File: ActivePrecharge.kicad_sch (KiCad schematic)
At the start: 52 parts, among them Con1 LED, J1 Conn_01x03, J2 Conn_01x02, J3 Conn_01x02, Q1 IRLML0030, U1 NCP785AH50T1G, U1I_TP1 TestPoint, U2 NCP785AH50T1G, U2I_TP1 TestPoint, U2O_TP1 TestPoint, U3 TLV9301xDCK, U4 TCMT1106

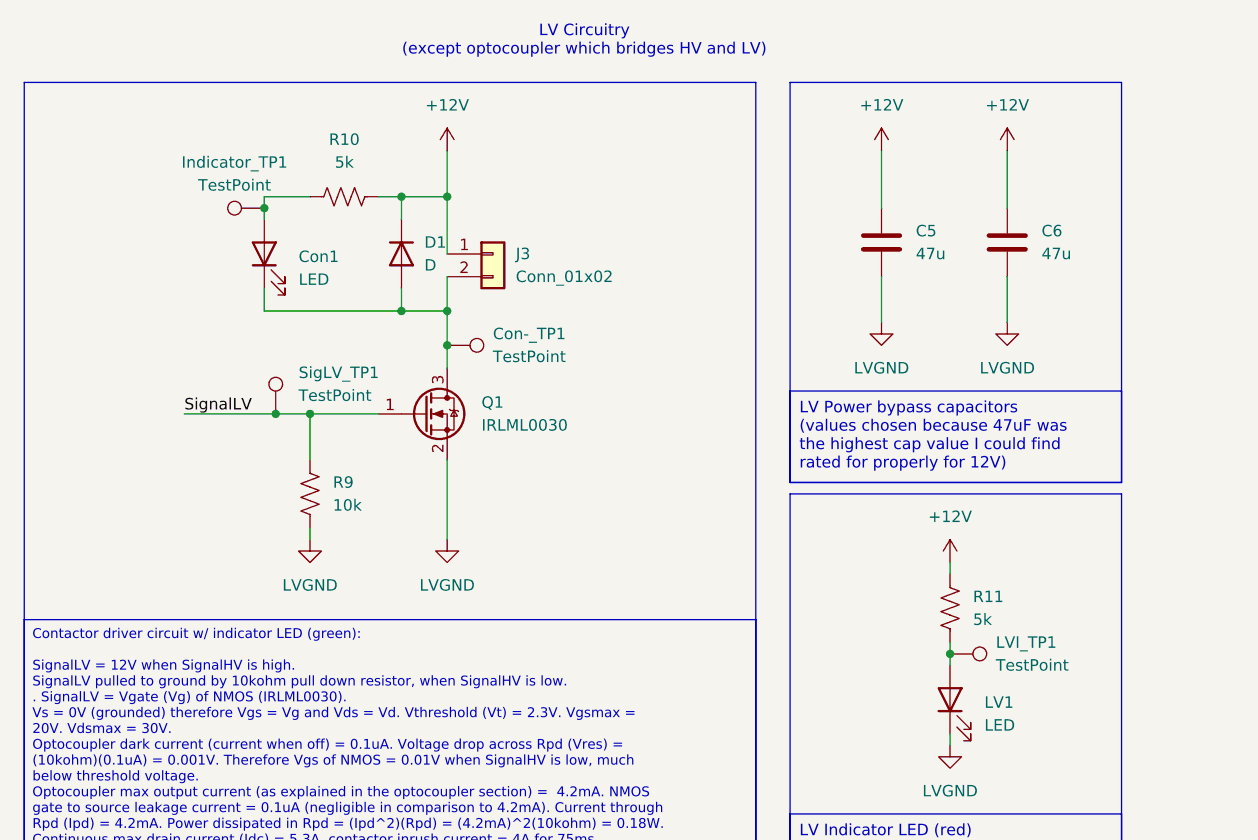
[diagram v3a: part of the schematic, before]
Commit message: improved tp labels, moved vias on the tp rather than next to the tp, removed ConIndVf and LVIndVf tp (pointless)
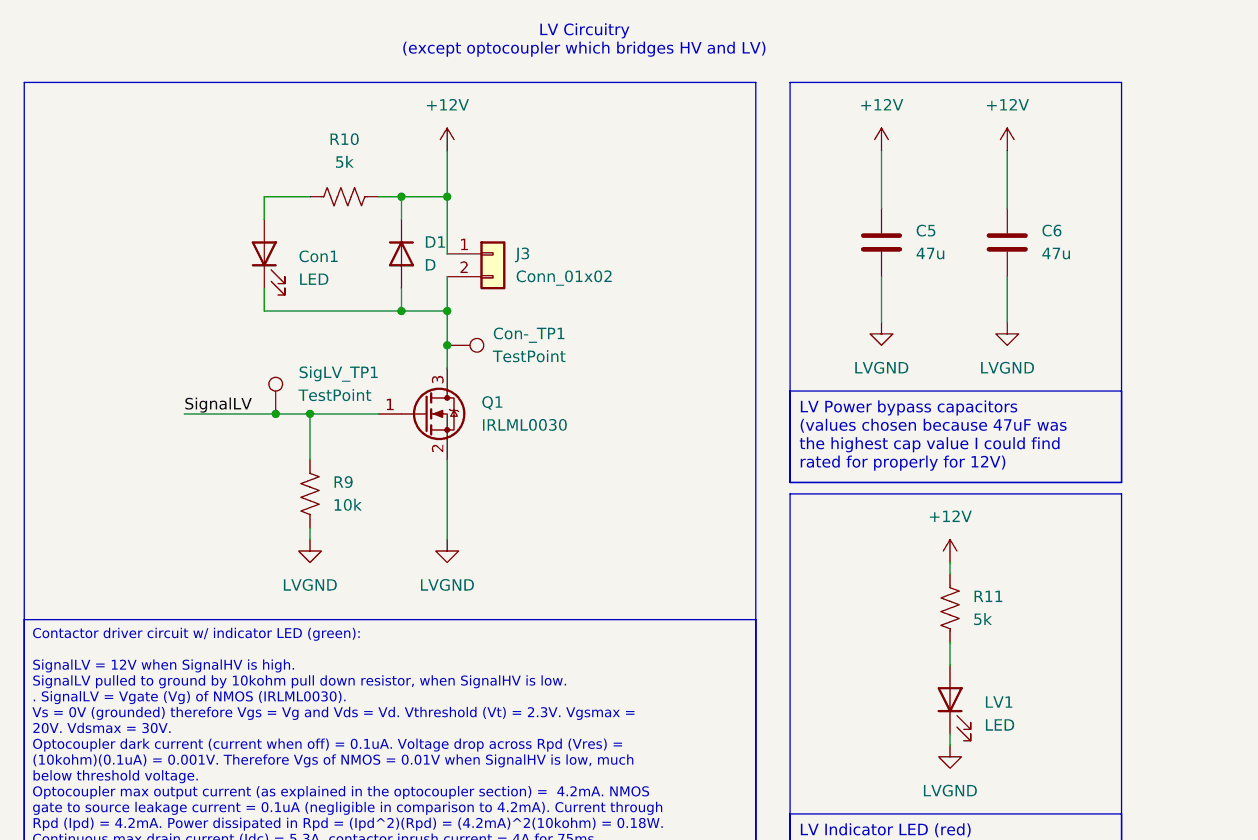
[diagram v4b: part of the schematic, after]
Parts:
- removed Indicator_TP1, LVI_TP1: TestPoint, Active-PrechargeLib:TestPoint_HEX_3mmID, symbol Connector:TestPoint
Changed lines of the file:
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@@
 	)
 	(junction
-		(at 262.89 85.09)
-		(diameter 0)
-		(color 0 0 0 0)
-	)
-	(junction
 		(at 69.85 134.62)
 		(diameter 0)
@@
 	)
 	(junction
-		(at 186.69 35.56)
-		(diameter 0)
-		(color 0 0 0 0)
-	)
-	(junction
 		(at 72.39 134.62)
 		(diameter 0)
@@
 	(wire
 		(pts
-			(xy 186.69 34.29) (xy 186.69 35.56)
+			(xy 186.69 34.29) (xy 186.69 36.83)
 		)
 		(stroke
@@
 	(wire
 		(pts
-			(xy 262.89 86.36) (xy 262.89 85.09)
-		)
-		(stroke
-			(width 0)
-			(type default)
-		)
-	)
-	(wire
-		(pts
 			(xy 256.54 125.73) (xy 256.54 128.27)
 		)
@@
 	(wire
 		(pts
-			(xy 262.89 83.82) (xy 262.89 85.09)
+			(xy 262.89 83.82) (xy 262.89 86.36)
 		)
 		(stroke
@@
 	(wire
 		(pts
-			(xy 186.69 35.56) (xy 186.69 36.83)
-		)
-		(stroke
-			(width 0)
-			(type default)
-		)
-	)
-	(wire
-		(pts
 			(xy 68.58 146.05) (xy 68.58 149.86)
 		)
@@
 	)
 	(symbol
-		(lib_id "Connector:TestPoint")
-		(at 262.89 85.09 270)
-		(unit 1)
-		(exclude_from_sim no)
-		(in_bom yes)
-		(on_board yes)
-		(dnp no)
-		(fields_autoplaced yes)
-		(property "Reference" "LVI_TP1"
-			(at 267.97 83.8199 90)
-			(effects
-				(font
-					(size 1.27 1.27)
-				)
-				(justify left)
-			)
-		)
-		(property "Value" "TestPoint"
-			(at 267.97 86.3599 90)
-			(effects
-				(font
-					(size 1.27 1.27)
-				)
-				(justify left)
-			)
-		)
-		(property "Footprint" "Active-PrechargeLib:TestPoint_HEX_3mmID"
-			(at 262.89 90.17 0)
-			(effects
-				(font
-					(size 1.27 1.27)
-				)
-				(hide yes)
-			)
-		)
-		(property "Datasheet" "~"
-			(at 262.89 90.17 0)
-			(effects
-				(font
-					(size 1.27 1.27)
-				)
-				(hide yes)
-			)
-		)
-		(property "Description" "test point"
-			(at 262.89 85.09 0)
-			(effects
-				(font
-					(size 1.27 1.27)
-				)
-				(hide yes)
-			)
-		)
-		(pin "1"
-		)
-		(instances
-			(project ""
-				(path "/b9847a31-2b3b-47ca-9561-fab506416f6d"
-					(reference "LVI_TP1")
-					(unit 1)
-				)
-			)
-		)
-	)
-	(symbol
 		(lib_id "Device:R_US")
 		(at 26.67 161.29 180)
@@
 					(unit 1)
 				)
-			)
-		)
-	)
-	(symbol
-		(lib_id "Connector:TestPoint")
-		(at 186.69 35.56 90)
-		(unit 1)
-		(exclude_from_sim no)
-		(in_bom yes)
-		(on_board yes)
-		(dnp no)
-		(fields_autoplaced yes)
-		(property "Reference" "Indicator_TP1"
-			(at 183.388 30.48 90)
-			(effects
-				(font
-					(size 1.27 1.27)
-				)
-			)
-		)
-		(property "Value" "TestPoint"
-			(at 183.388 33.02 90)
-			(effects
-				(font
-					(size 1.27 1.27)
-				)
-			)
-		)
-		(property "Footprint" "Active-PrechargeLib:TestPoint_HEX_3mmID"
-			(at 186.69 30.48 0)
-			(effects
-				(font
-					(size 1.27 1.27)
-				)
-				(hide yes)
-			)
-		)
-		(property "Datasheet" "~"
-			(at 186.69 30.48 0)
-			(effects
-				(font
-					(size 1.27 1.27)
-				)
-				(hide yes)
-			)
-		)
-		(property "Description" "test point"
-			(at 186.69 35.56 0)
-			(effects
-				(font
-					(size 1.27 1.27)
-				)
-				(hide yes)
-			)
-		)
-		(pin "1"
-		)
-		(instances
-			(project ""
-				(path "/b9847a31-2b3b-47ca-9561-fab506416f6d"
-					(reference "Indicator_TP1")
-					(unit 1)
-				)

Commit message: redid sch and layout w/ reverse polarity protection on HV and LV inputs, low pass filter on comparator inputs, hystersesis on comparator
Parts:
- added C1, C2: 1uF, Capacitor_SMD:C_0805_2012Metric, symbol Device:C
- added D1, D2, D3: RSX068MP2STR, Diode_SMD:D_SOD-123F, symbol Device:D_Schottky
- added D4: BZT52-B12-QX, Active-PrechargeLib:BZT52B12QX, symbol Device:D_Zener
- added Q1: PMV35EPER, Package_TO_SOT_SMD:SOT-23-3, symbol Simulation_SPICE:PMOS
- added R13: 100k, Resistor_SMD:R_0805_2012Metric, symbol Device:R_US
- added R5: 44.2k, Resistor_SMD:R_0805_2012Metric, symbol Device:R_US
- renumbered C1 to C3, C2 to C4, C3 to C5, C4 to C6, C5 to C7, C6 to C8, D1 to D5, Q1 to Q2, R9 to R10, R10 to R11, R11 to R12, R5 to R6, R6 to R7, R7 to R9
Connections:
- net +12V: now also Q1.1 (D); no longer 12V_TP1.1, D5.1 (K), J3.1 (Pin_1), R11.2, R12.1
- net HVGND: now also D1.1 (K); no longer C3.2, C4.1, C5.2, C6.1, HV1.1 (K), HVG_TP1.1, R2.2, R4.2, U1.2 (GND), U2.2 (GND), U3.2 (V-), U4.2
- net HVIn: now also J1.3 (Pin_3), D3.2 (A); no longer J1.2 (Pin_2), R3.1
- net HVRef: now also J1.2 (Pin_2), D2.2 (A); no longer J1.3 (Pin_3), R1.1, R6.1, R7.2
- net LVGND: now also R13.1
- net SignalHV: now also U4.2, R5.2; no longer R8.1
- net Vcc+: now also R8.2
- net Vin: now also U3.3 (-), C2.1; no longer U3.1 (+)
- net Vref: now also U3.1 (+), C1.1, R5.1; no longer U3.3 (-)
- net at OptVf_TP1.1, U4.1: now also R8.1; no longer R8.2
- new net: D4.2 (A), Q1.2 (G), R13.2
- new net HGND: C1.2, C2.2, C3.2, C4.1, C5.2, C6.1, D1.2 (A), HV1.1 (K), HVG_TP1.1, R2.2, R4.2, U1.2 (GND), U2.2 (GND), U3.2 (V-)
- new net HIn: D3.1 (K), R3.1
- new net HRef: D2.1 (K), R1.1, R6.1, R7.2
- new net LV+: 12V_TP1.1, D4.1 (K), D5.1 (K), J3.1 (Pin_1), Q1.3 (S), R11.2, R12.1
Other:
- added sheet Untitled Sheet (untitled.kicad_sch)
- moved on the sheet: 12V_TP1, C3, C4, C5, C6, HV1, HVG_TP1, HVI_TP1, HVI_TP2, HVR_TP1, IN_TP1, J1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

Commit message: updated sch explinations with new additions from today's workday
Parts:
- R1: value 110k -> 120k
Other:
- moved on the sheet: 12V_TP1, C1, C2, C3, C4, C5, C6, C7, C8, Con-_TP1, Con1, D1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

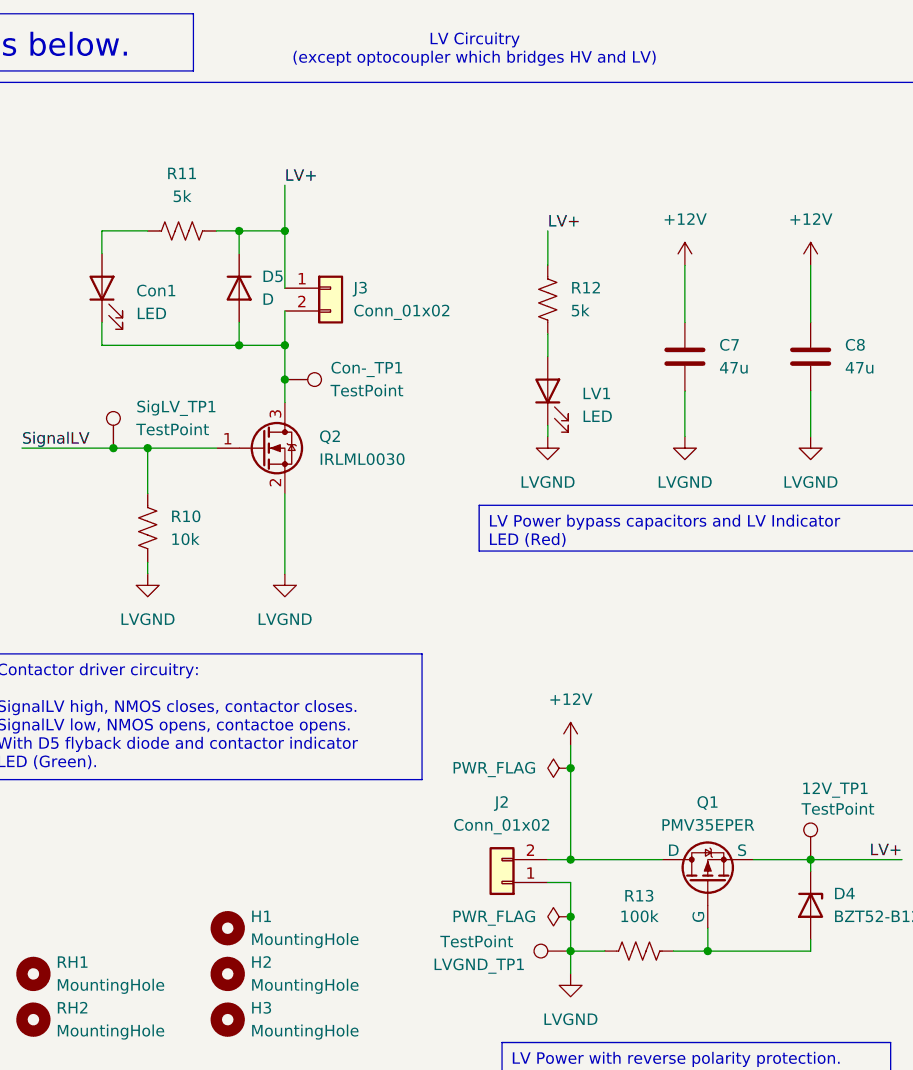
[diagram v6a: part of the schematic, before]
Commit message: fixed pmos orientation on LV reverse polarity protection, was s and d were backwards
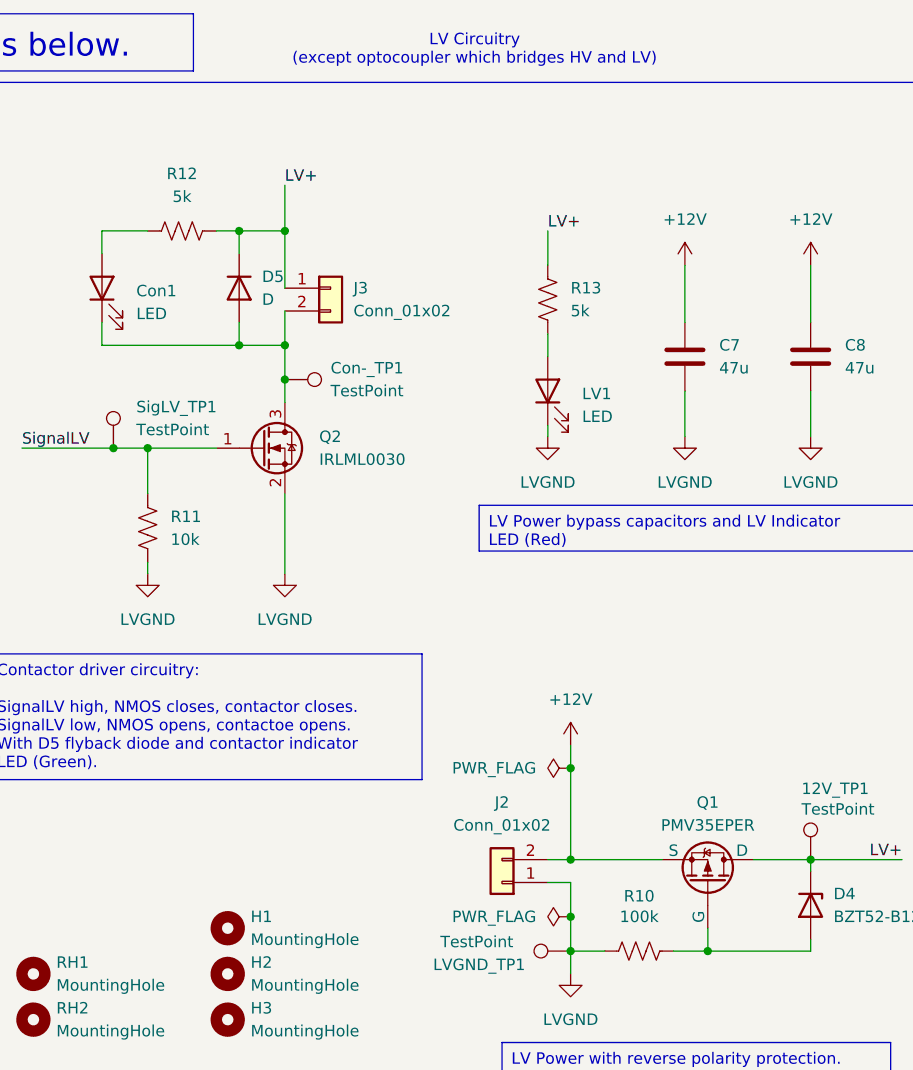
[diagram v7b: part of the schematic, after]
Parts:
- renumbered R13 to R10, R10 to R11, R11 to R12, R12 to R13
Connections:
- net +12V: now also Q1.3 (S); no longer Q1.1 (D)
- net LV+: now also Q1.1 (D); no longer Q1.3 (S)
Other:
- moved on the sheet: Q1
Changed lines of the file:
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@@
 	(symbol
 		(lib_id "Simulation_SPICE:PMOS")
-		(at 250.19 109.22 90)
+		(at 250.19 109.22 270)
+		(mirror x)
 		(unit 1)
 		(exclude_from_sim no)
@@
 		(on_board yes)
 		(dnp no)
-		(fields_autoplaced yes)
 		(property "Reference" "Q1"
 			(at 250.19 100.33 90)
@@
 		)
 		(property "Footprint" "Package_TO_SOT_SMD:SOT-23-3"
-			(at 247.65 104.14 0)
+			(at 252.73 104.14 0)
 			(effects
 				(font
@@
 		)
 		(property "Datasheet" "https://ngspice.sourceforge.io/docs/ngspice-html-manual/manual.xhtml#cha_MOSFETs"
-			(at 262.89 109.22 0)
+			(at 237.49 109.22 0)
 			(effects
 				(font
@@
 		)
 		(property "Sim.Device" "PMOS"
-			(at 267.335 109.22 0)
+			(at 233.045 109.22 0)
 			(effects
 				(font
@@
 		)
 		(property "Sim.Type" "VDMOS"
-			(at 269.24 109.22 0)
+			(at 231.14 109.22 0)
 			(effects
 				(font
@@
 		)
 		(property "Sim.Pins" "1=D 2=G 3=S"
-			(at 265.43 109.22 0)
+			(at 234.95 109.22 0)
 			(effects
 				(font
@@
 		(on_board yes)
 		(dnp no)
-		(property "Reference" "R13"
+		(property "Reference" "R10"
 			(at 242.57 110.744 90)
 			(effects
@@
 			(project ""
 				(path "/b9847a31-2b3b-47ca-9561-fab506416f6d"
-					(reference "R13")
+					(reference "R10")
 					(unit 1)
 				)
@@
 		(on_board yes)
 		(dnp no)
-		(property "Reference" "R10"
+		(property "Reference" "R11"
 			(at 190.5 68.5799 0)
 			(effects
@@
 			(project ""
 				(path "/b9847a31-2b3b-47ca-9561-fab506416f6d"
-					(reference "R10")
+					(reference "R11")
 					(unit 1)
 				)
@@
 		(dnp no)
 		(fields_autoplaced yes)
-		(property "Reference" "R12"
+		(property "Reference" "R13"
 			(at 234.95 43.1799 0)
 			(effects
@@
 			(project ""
 				(path "/b9847a31-2b3b-47ca-9561-fab506416f6d"
-					(reference "R12")
+					(reference "R13")
 					(unit 1)
 				)
@@
 		(dnp no)
 		(fields_autoplaced yes)
-		(property "Reference" "R11"
+		(property "Reference" "R12"
 			(at 191.77 30.48 90)
 			(effects
@@
 			(project ""
 				(path "/b9847a31-2b3b-47ca-9561-fab506416f6d"
-					(reference "R11")
+					(reference "R12")
 					(unit 1)
 				)

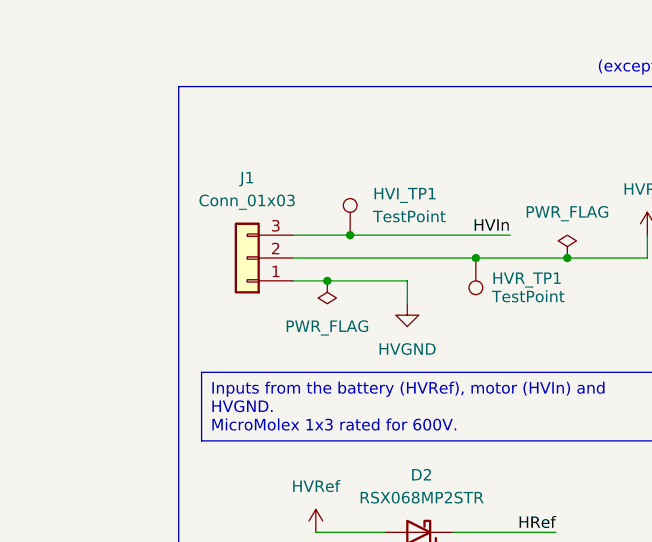
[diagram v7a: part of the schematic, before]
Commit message: HV Layout w/ components on the back
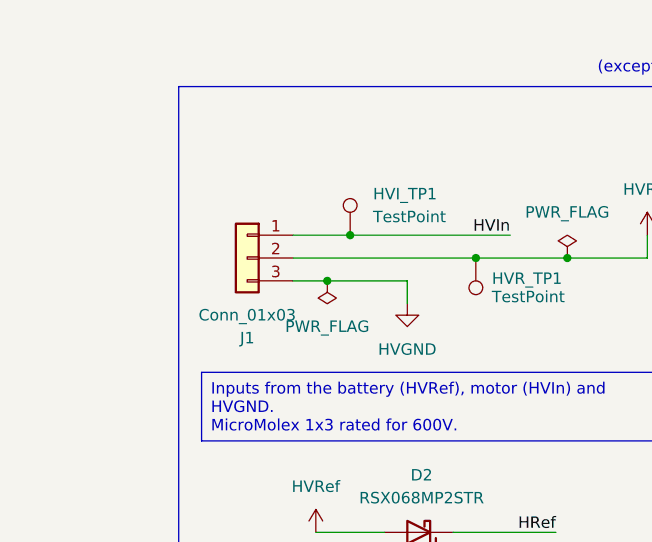
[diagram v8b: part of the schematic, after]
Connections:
- net HVGND: now also J1.3 (Pin_3); no longer J1.1 (Pin_1)
- net HVIn: now also J1.1 (Pin_1); no longer J1.3 (Pin_3)
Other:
- moved on the sheet: J1
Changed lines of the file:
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@@
 	(symbol
 		(lib_id "Connector_Generic:Conn_01x03")
-		(at 25.4 39.37 180)
+		(at 25.4 39.37 0)
+		(mirror y)
 		(unit 1)
 		(exclude_from_sim no)
@@
 		(on_board yes)
 		(dnp no)
-		(fields_autoplaced yes)
 		(property "Reference" "J1"
-			(at 25.4 30.48 0)
+			(at 25.4 48.26 0)
 			(effects
 				(font
@@
 		)
 		(property "Value" "Conn_01x03"
-			(at 25.4 33.02 0)
+			(at 25.4 45.72 0)
 			(effects
 				(font
